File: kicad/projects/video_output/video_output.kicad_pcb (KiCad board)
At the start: 2 copper layers, 203.2 x 97.8 mm, 64 parts, among them J1 peripheral_addr_bus_connector, J2 peripheral_aux_connector, J3 peripheral_membank_connector, J4 Conn_01x16_Socket, J5 Conn_01x16_Socket, J6 Conn_02x06_Odd_Even, J7 DE15_Receptacle_HighDensity, J8 video_aux, J9 Conn_01x04_Socket, U1 628128_DIP32_SSOP32, U10 74HC157, U11 74HC157, U12 74HC10, U13 74HC02, U14 74HC08, U15 74HC123, U16 74HC32, U17 74HC04, U2 628128_DIP32_SSOP32, U3 74HC245, U4 74HC245, U5 74HC245, U6 74HC245, U7 74HC574, U8 74HC245, U9 74HC574

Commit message: Start PCB for video timing.
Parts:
- added C15: C, Capacitor_THT:C_Disc_D5.0mm_W2.5mm_P5.00mm, F.Cu at (188.0, 31.5)
- added C16: C, Capacitor_THT:C_Disc_D5.0mm_W2.5mm_P5.00mm, F.Cu at (188.0, 35.6)
- added C17: C, Capacitor_THT:C_Disc_D5.0mm_W2.5mm_P5.00mm, F.Cu at (205.7, 68.6)
- added C18: C, Capacitor_THT:C_Disc_D5.0mm_W2.5mm_P5.00mm, F.Cu at (157.5, 68.6)
- added C19: C, Capacitor_THT:C_Disc_D5.0mm_W2.5mm_P5.00mm, F.Cu at (213.4, 111.8)
- added C20: C, Capacitor_THT:C_Disc_D5.0mm_W2.5mm_P5.00mm, F.Cu at (170.2, 111.8)
- moved C14 173.8 mm to (127.0, 78.7), turned to 90 degrees
- moved C11 173.3 mm to (127.0, 60.9), turned to 90 degrees
- moved C9 166.4 mm to (127.0, 132.0), turned to 90 degrees
- moved C8 164.0 mm to (127.0, 114.2), turned to 90 degrees
- moved C6 163.0 mm to (127.0, 96.4), turned to 90 degrees
- moved C13 149.2 mm to (101.6, 78.7), turned to 90 degrees
- moved C10 145.9 mm to (99.1, 60.9), turned to 90 degrees
- moved C5 138.1 mm to (101.6, 96.4), turned to 90 degrees
- moved C7 132.1 mm to (94.0, 114.2), turned to 90 degrees
- moved C12 125.1 mm to (76.2, 78.7), turned to 90 degrees
- moved C4 113.6 mm to (76.2, 96.4), turned to 90 degrees
- moved RN5 102.1 mm to (154.9, 121.9), turned to 180 degrees
- moved U8 77.9 mm to (132.1, 134.6), turned to 90 degrees
- moved U9 58.9 mm to (132.1, 116.8), turned to 90 degrees
- moved C3 37.5 mm to (124.5, 68.6), turned to 180 degrees
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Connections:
- U12 pad 14: unconnected-(U12D-VCC-Pad14) -> VCC
- U12 pad 7: unconnected-(U12D-GND-Pad7) -> GND
- U13 pad 14: unconnected-(U13E-VCC-Pad14) -> VCC
- U13 pad 7: unconnected-(U13E-GND-Pad7) -> GND
- U14 pad 14: unconnected-(U14E-VCC-Pad14) -> VCC
- U14 pad 7: unconnected-(U14E-GND-Pad7) -> GND
- U15 pad 16: unconnected-(U15C-VCC-Pad16) -> VCC
- U15 pad 8: unconnected-(U15C-GND-Pad8) -> GND
- U16 pad 14: unconnected-(U16E-VCC-Pad14) -> VCC
- U16 pad 7: unconnected-(U16E-GND-Pad7) -> GND
- U17 pad 14: unconnected-(U17G-VCC-Pad14) -> VCC
- U17 pad 7: unconnected-(U17G-GND-Pad7) -> GND
- U8 pad 1: VCC -> unconnected-(U8-DIR-Pad1)
- U8 pad 11: /VSYNC_OUT -> /VSYNC_CLOCKED
- U8 pad 12: /HSYNC_OUT -> /HSYNC_CLOCKED
- U8 pad 13: /PIX_B_01_OUT -> /PIX_B_01_CLOCKED
- U8 pad 14: /PIX_B_00_OUT -> /PIX_B_00_CLOCKED
- U8 pad 15: /PIX_G_01_OUT -> /PIX_G_01_CLOCKED
- U8 pad 16: /PIX_G_00_OUT -> /PIX_G_00_CLOCKED
- U8 pad 17: /PIX_R_01_OUT -> /PIX_R_01_CLOCKED
- U8 pad 18: /PIX_R_00_OUT -> /PIX_R_00_CLOCKED
- U8 pad 2: /PIX_R_00_CLOCKED -> /PIX_R_00_OUT
- U8 pad 3: /PIX_R_01_CLOCKED -> /PIX_R_01_OUT
- U8 pad 4: /PIX_G_00_CLOCKED -> /PIX_G_00_OUT
- U8 pad 5: /PIX_G_01_CLOCKED -> /PIX_G_01_OUT
- U8 pad 6: /PIX_B_00_CLOCKED -> /PIX_B_00_OUT
- U8 pad 7: /PIX_B_01_CLOCKED -> /PIX_B_01_OUT
- U8 pad 8: /HSYNC_CLOCKED -> /HSYNC_OUT
- U8 pad 9: /VSYNC_CLOCKED -> /VSYNC_OUT
- U9 pad 12: unconnected-(U9-Q7-Pad12) -> GND
- U9 pad 13: unconnected-(U9-Q6-Pad13) -> GND
- U9 pad 14: /PIX_B_01_CLOCKED -> /PIX_B_01
- U9 pad 15: /PIX_B_00_CLOCKED -> /PIX_B_00
- U9 pad 16: /PIX_G_01_CLOCKED -> /PIX_G_01
- U9 pad 17: /PIX_G_00_CLOCKED -> /PIX_G_00
- U9 pad 18: /PIX_R_01_CLOCKED -> /PIX_R_01
- U9 pad 19: /PIX_R_00_CLOCKED -> /PIX_R_00
- U9 pad 2: /PIX_R_00 -> /PIX_R_00_CLOCKED
- U9 pad 3: /PIX_R_01 -> /PIX_R_01_CLOCKED
- U9 pad 4: /PIX_G_00 -> /PIX_G_00_CLOCKED
- U9 pad 5: /PIX_G_01 -> /PIX_G_01_CLOCKED
- U9 pad 6: /PIX_B_00 -> /PIX_B_00_CLOCKED
- U9 pad 7: /PIX_B_01 -> /PIX_B_01_CLOCKED
- U9 pad 8: GND -> unconnected-(U9-D6-Pad8)
- U9 pad 9: GND -> unconnected-(U9-D7-Pad9)

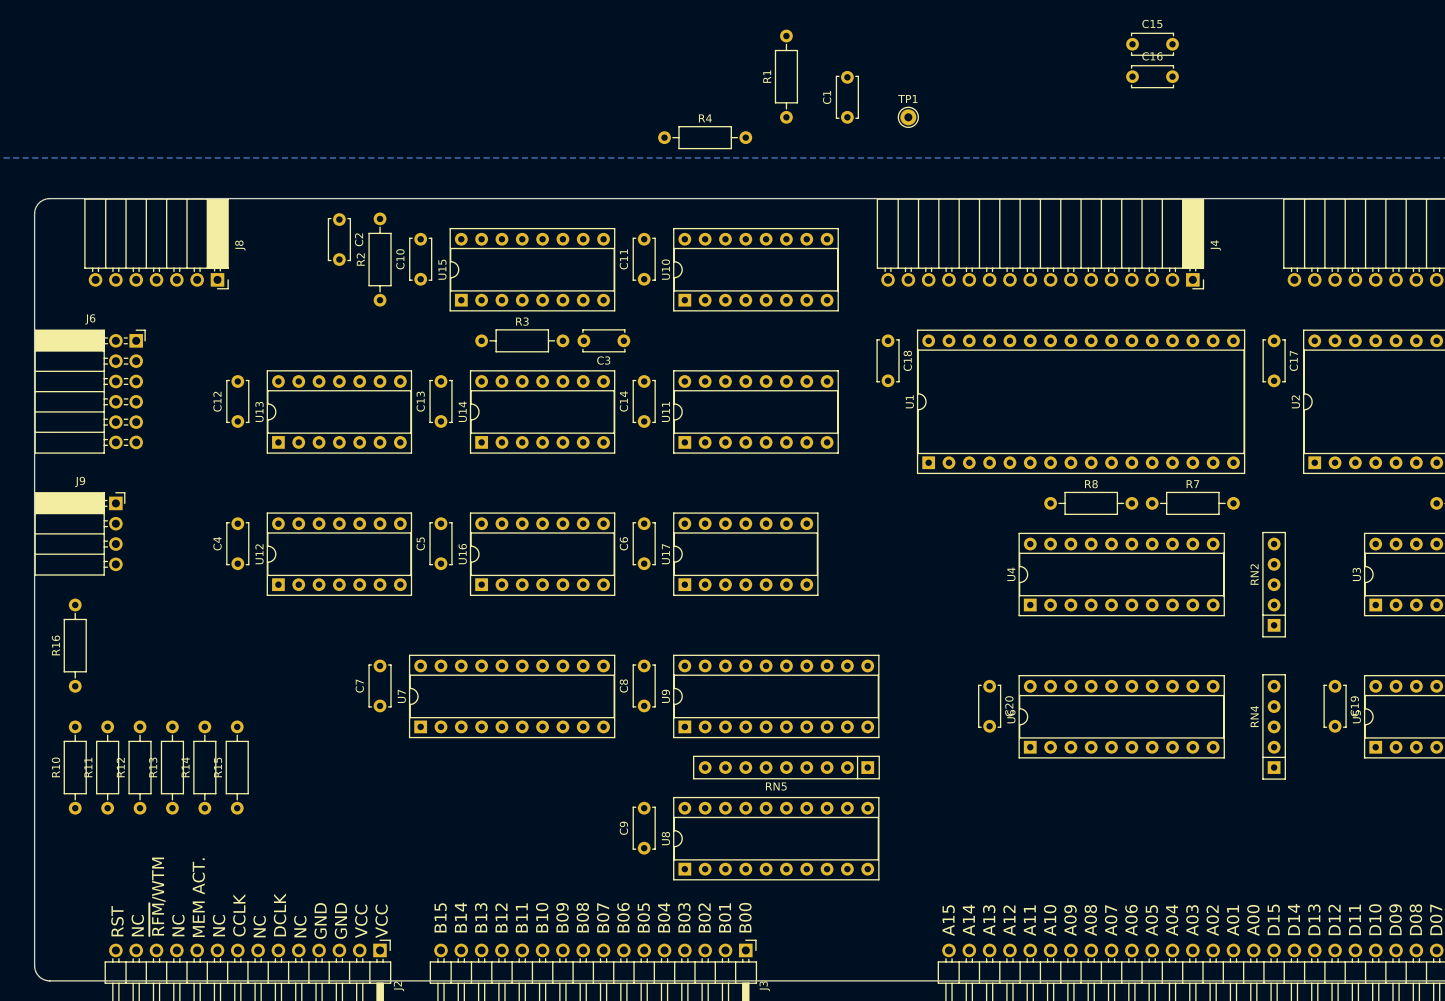
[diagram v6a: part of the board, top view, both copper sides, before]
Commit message: Start work on output PCB.
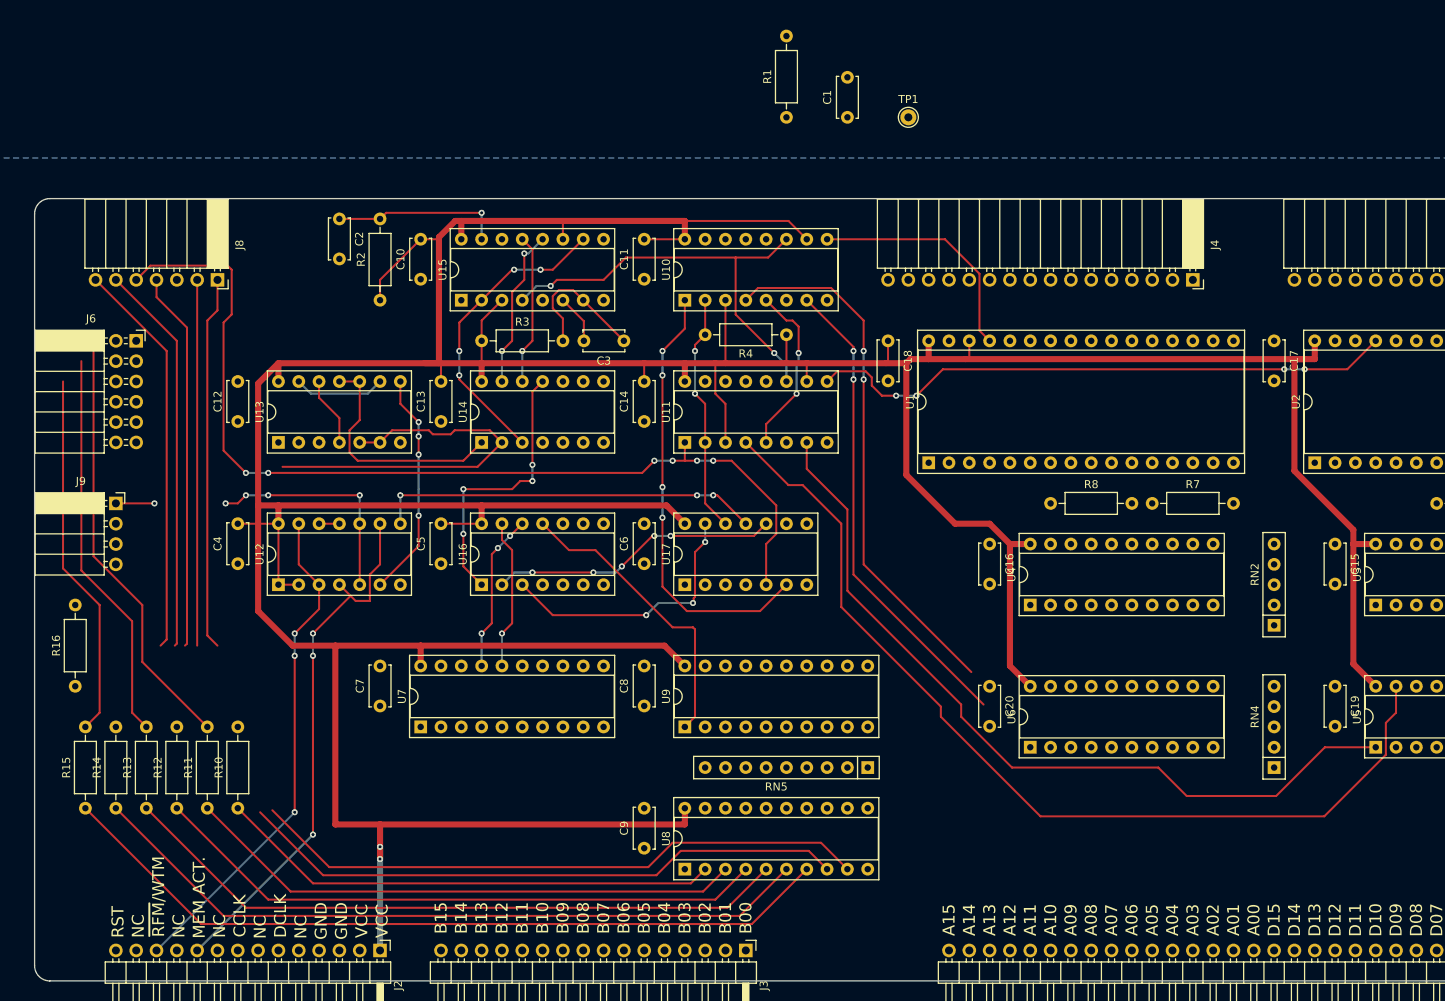
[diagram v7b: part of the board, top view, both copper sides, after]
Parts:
- moved C15 67.4 mm to (213.4, 94.0), turned to -90 degrees
- moved C16 61.1 mm to (170.2, 94.0), turned to -90 degrees
- moved R4 29.0 mm to (144.8, 67.8), turned to 180 degrees
- moved R10 20.3 mm to (76.2, 127.0)
- moved R15 19.0 mm to (57.1, 127.0)
- moved R11 12.5 mm to (72.4, 127.0)
- moved R14 11.1 mm to (61.0, 127.0)
- moved R12 4.60 mm to (68.6, 127.0)
- moved R13 3.26 mm to (64.8, 127.0)
- moved C2 0.08 mm to (88.9, 53.3)
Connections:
- J1 pad 10: /DATA_BUS_09 -> unconnected-(J1-D_09-Pad10)
- J1 pad 11: /DATA_BUS_10 -> unconnected-(J1-D_10-Pad11)
- J1 pad 12: /DATA_BUS_11 -> unconnected-(J1-D_11-Pad12)
- J1 pad 13: /DATA_BUS_12 -> unconnected-(J1-D_12-Pad13)
- J1 pad 14: /DATA_BUS_13 -> unconnected-(J1-D_13-Pad14)
- J1 pad 15: /DATA_BUS_14 -> unconnected-(J1-D_14-Pad15)
- J1 pad 16: /DATA_BUS_15 -> unconnected-(J1-D_15-Pad16)
- J1 pad 17: /ADDR_BUS_00 -> unconnected-(J1-A_00-Pad17)
- J1 pad 18: /ADDR_BUS_01 -> unconnected-(J1-A_01-Pad18)
- J1 pad 19: /ADDR_BUS_02 -> unconnected-(J1-A_02-Pad19)
- J1 pad 20: /ADDR_BUS_03 -> unconnected-(J1-A_03-Pad20)
- J1 pad 21: /ADDR_BUS_04 -> unconnected-(J1-A_04-Pad21)
- J1 pad 22: /ADDR_BUS_05 -> unconnected-(J1-A_05-Pad22)
- J1 pad 23: /ADDR_BUS_06 -> unconnected-(J1-A_06-Pad23)
- J1 pad 24: /ADDR_BUS_07 -> unconnected-(J1-A_07-Pad24)
- J1 pad 25: /ADDR_BUS_08 -> unconnected-(J1-A_08-Pad25)
- J1 pad 26: /ADDR_BUS_09 -> unconnected-(J1-A_09-Pad26)
- J1 pad 27: /ADDR_BUS_10 -> unconnected-(J1-A_10-Pad27)
- J1 pad 28: /ADDR_BUS_11 -> unconnected-(J1-A_11-Pad28)
- J1 pad 29: /ADDR_BUS_12 -> unconnected-(J1-A_12-Pad29)
- J1 pad 30: /ADDR_BUS_13 -> unconnected-(J1-A_13-Pad30)
- J1 pad 31: /ADDR_BUS_14 -> unconnected-(J1-A_14-Pad31)
- J1 pad 32: /ADDR_BUS_15 -> unconnected-(J1-A_15-Pad32)
- J1 pad 8: /DATA_BUS_07 -> unconnected-(J1-D_07-Pad8)
- J1 pad 9: /DATA_BUS_08 -> unconnected-(J1-D_08-Pad9)
- J2 pad 14: /RESET -> unconnected-(J2-RST-Pad14)
- J2 pad 8: /CTL_CLK -> unconnected-(J2-CCLK-Pad8)
- J3 pad 1: /BANK_BUS_00 -> unconnected-(J3-B_00-Pad1)
- J3 pad 10: /BANK_BUS_09 -> unconnected-(J3-B_09-Pad10)
- J3 pad 11: /BANK_BUS_10 -> unconnected-(J3-B_10-Pad11)
- J3 pad 12: /BANK_BUS_11 -> unconnected-(J3-B_11-Pad12)
- J3 pad 13: /BANK_BUS_12 -> unconnected-(J3-B_12-Pad13)
- J3 pad 14: /BANK_BUS_13 -> unconnected-(J3-B_13-Pad14)
- J3 pad 15: /BANK_BUS_14 -> unconnected-(J3-B_14-Pad15)
- J3 pad 16: /BANK_BUS_15 -> unconnected-(J3-B_15-Pad16)
- J3 pad 2: /BANK_BUS_01 -> unconnected-(J3-B_01-Pad2)
- J3 pad 3: /BANK_BUS_02 -> unconnected-(J3-B_02-Pad3)
- J3 pad 4: /BANK_BUS_03 -> unconnected-(J3-B_03-Pad4)
- J3 pad 5: /BANK_BUS_04 -> unconnected-(J3-B_04-Pad5)
- J3 pad 6: /BANK_BUS_05 -> unconnected-(J3-B_05-Pad6)
- J3 pad 7: /BANK_BUS_06 -> unconnected-(J3-B_06-Pad7)
- J3 pad 8: /BANK_BUS_07 -> unconnected-(J3-B_07-Pad8)
- J3 pad 9: /BANK_BUS_08 -> unconnected-(J3-B_08-Pad9)
- U13 pad 2: unconnected-(U13-Pad2) -> GND
- U13 pad 3: unconnected-(U13-Pad3) -> GND
- U14 pad 10: unconnected-(U14-Pad10) -> GND
- U14 pad 4: unconnected-(U14-Pad4) -> GND
- U14 pad 5: unconnected-(U14-Pad5) -> GND
- U14 pad 9: unconnected-(U14-Pad9) -> GND
- U16 pad 10: unconnected-(U16-Pad10) -> GND
- U16 pad 4: unconnected-(U16-Pad4) -> GND
- U16 pad 5: unconnected-(U16-Pad5) -> GND
- U16 pad 9: unconnected-(U16-Pad9) -> GND
- U17 pad 1: unconnected-(U17-Pad1) -> GND
- U17 pad 3: unconnected-(U17-Pad3) -> GND
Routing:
- net VCC: track 0.00 -> 630.2 mm, vias 0 -> 2
- net /BANK_SEL: track 0.00 -> 121.8 mm, vias 0 -> 6
- net /A_DATA_BUF_~{OE}: track 0.00 -> 118.5 mm
- net /A_DATA_BUF_DIR: track 0.00 -> 100.7 mm
- net /PIX_B_01_OUT: track 0.00 -> 99.0 mm
- net /PIX_B_00_OUT: track 0.00 -> 91.8 mm
- net /PIX_G_01_OUT: track 0.00 -> 84.6 mm
- net /VSYNC_OUT: track 0.00 -> 77.5 mm
- net /PIX_G_00_OUT: track 0.00 -> 77.4 mm
- net /HSYNC_OUT: track 0.00 -> 76.3 mm
- net /A_RAM_~{WE}: track 0.00 -> 73.8 mm, vias 0 -> 4
- net /PIX_R_01_OUT: track 0.00 -> 70.2 mm
- net /MEM_ACT: track 0.00 -> 67.1 mm, vias 0 -> 3
- net /B_DATA_BUF_~{OE}: track 0.00 -> 66.6 mm, vias 0 -> 2
- net /PIX_R_00_OUT: track 0.00 -> 63.0 mm
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
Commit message: Part way through output PCB.
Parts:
- moved R8 33.3 mm to (199.4, 63.5), turned to 90 degrees
- moved R7 29.0 mm to (204.5, 63.5), turned to 90 degrees
- moved R5 28.4 mm to (251.5, 63.5), turned to 90 degrees
- moved R6 22.9 mm to (248.9, 88.9), turned to 180 degrees
- moved R16 10.2 mm to (55.9, 101.6), turned to -90 degrees
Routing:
- net /PIXEL_CLK_MOD: track 47.4 -> 136.6 mm, vias 0 -> 4
- net /DATA_CLK: track 48.2 -> 125.4 mm, vias 0 -> 5
- net /HSYNC_OUT: track 76.3 -> 140.1 mm
- net /VSYNC_OUT: track 77.5 -> 138.7 mm, vias 0 -> 2
- net /VSYNC_CLOCKED: track 0.00 -> 59.8 mm, vias 0 -> 3
- net /HSYNC_CLOCKED: track 0.00 -> 58.2 mm, vias 0 -> 3
- net /VBLANK: track 49.7 -> 99.1 mm
- net VCC: track 630.2 -> 676.6 mm, vias 2 -> 6
- net /HBLANK: track 49.0 -> 93.8 mm
- net /VSYNC: track 45.7 -> 85.3 mm
- net /HSYNC: track 46.8 -> 80.6 mm
- net /PIX_A_G_01: track 0.00 -> 33.8 mm
- net /PIX_A_B_01: track 0.00 -> 33.8 mm
- net /PIX_A_B_00: track 0.00 -> 33.8 mm
- net /ROW_A_02: track 0.00 -> 30.6 mm, vias 0 -> 2
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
